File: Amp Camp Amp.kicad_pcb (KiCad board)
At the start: 2 copper layers, 120 x 111.2 mm, 58 parts, among them Q1 IRFP240, Q2 IRFP240, Q3 ZTX450, Q4 2SK170, SW1 MONO, T1 IN_L_P5.00mm, T2 OUT_L_P5.00mm, T3 S+24V_IN_L_P5.00mm, T4 IN_L_P5.00mm, T5 IN_R_P5.00mm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

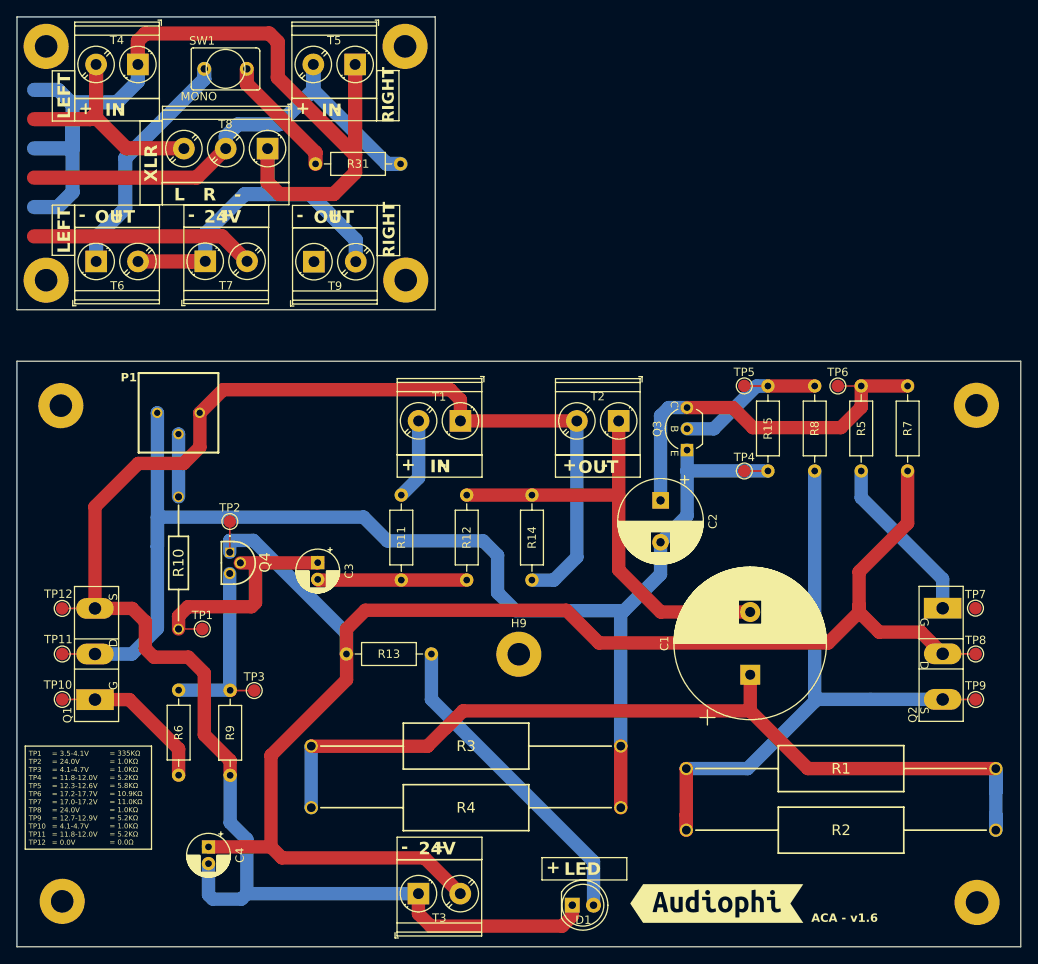
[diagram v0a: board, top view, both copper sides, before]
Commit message: Updated the board to version 1.8
List of all differences between V1.6 and V1.8:

Rear switch is a 3 position DPDT instead of 2 position, necessitating a change in wiring
Rear panel is printed with a connection diagram
Chassis rails are improved using weld nuts and secured by bolts
Blade terminals are included for the front power switch
Longer wire
LED resistors have been changed from 10k to 33.2k to reduce LED brightness
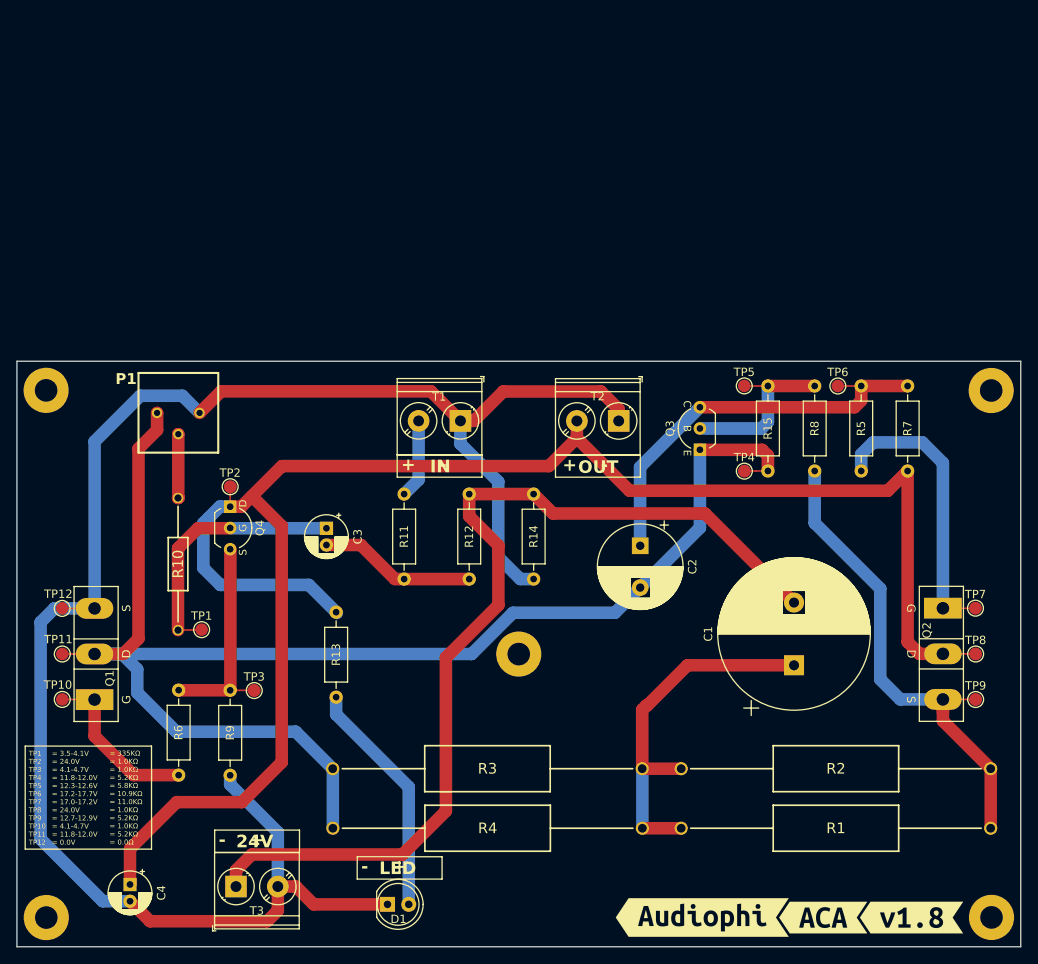
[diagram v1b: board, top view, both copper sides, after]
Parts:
- removed H6, H7, H8, H9: MountingHole_Pad, MountingHole:MountingHole_2.7mm_Pad
- removed R31: 39k, Resistor_THT:R_Axial_DIN0207_L6.3mm_D2.5mm_P10.16mm_Horizontal
- removed SW1: MONO, PCM_4ms_Switch:Switch_Toggle_SPST_SubMini
- removed T4: IN_L_P5.00mm, TerminalBlock_Phoenix:TerminalBlock_Phoenix_PT-1,5-2-5.0-H_1x02_P5.00mm_Horizontal
- removed T5: IN_R_P5.00mm, TerminalBlock_Phoenix:TerminalBlock_Phoenix_PT-1,5-2-5.0-H_1x02_P5.00mm_Horizontal
- removed T6: OUT_L_P5.00mm, TerminalBlock_Phoenix:TerminalBlock_Phoenix_PT-1,5-2-5.0-H_1x02_P5.00mm_Horizontal
- removed T7: IN+24V_P5.00mm, TerminalBlock_Phoenix:TerminalBlock_Phoenix_PT-1,5-2-5.0-H_1x02_P5.00mm_Horizontal
- removed T8: XLR_IN_P5.00mm, TerminalBlock_Phoenix:TerminalBlock_Phoenix_PT-1,5-3-5.0-H_1x03_P5.00mm_Horizontal
- removed T9: OUT_R_P5.00mm, TerminalBlock_Phoenix:TerminalBlock_Phoenix_PT-1,5-2-5.0-H_1x02_P5.00mm_Horizontal
- removed VR1: 3386P-1-502LF, Samacsys:3386P_1
- added P1: 3386P-1-502LF, Samacsys:3386P_1, B.Cu at (118.9, 85.2)
- added kibuzzard-674CED68: G***, kibuzzard-674CED68, F.Cu at (200.8, 150.3)
- added kibuzzard-674D924F: G***, kibuzzard-674D924F, F.Cu at (211.4, 150.3)
- Q4: value 2SK170 -> TO-92_Inline_Wide_EBC; footprint Samacsys:2SK170 -> PCM_Package_TO_SOT_THT_AKL:TO-92_Inline_Wide_EBC
- R13: value 10k Ω -> 33.2k
- T2: value OUT_L_P5.00mm -> S+24V_IN_L_P5.00mm
- T3: value S+24V_IN_L_P5.00mm -> OUT_L_P5.00mm
- TP11: value 11.8-12V/5.2KΩ -> 12V (BIAS)
- TP12: value 0V/0Ω -> 0V
- TP4: value 11.8-12V -> 12V
- TP5: value 12.3-12.6V -> 12.6V
- TP7: value 17.0-17.2V -> 17.2-17.7V
- TP9: value 12.7-12.9V -> 12.9V
- moved H4 103.5 mm to (220.9, 150.2)
- moved H2 81.3 mm to (220.9, 87.3)
- moved H3 76.2 mm to (107.9, 150.3)
- moved H5 62.3 mm to (164.4, 118.8)
- moved H1 41.1 mm to (107.9, 87.2)
- moved R4 39.7 mm to (179.2, 139.6), turned to 180 degrees
- moved R3 39.7 mm to (179.2, 132.5), turned to 180 degrees
- moved R2 37.1 mm to (220.8, 132.5), turned to 180 degrees
- moved R1 37.1 mm to (220.8, 139.6), turned to 180 degrees
- moved D1 22.1 mm to (148.7, 148.7)
- moved T3 21.8 mm to (130.6, 146.6)
- moved C4 10.4 mm to (117.9, 146.3)
- moved C2 5.94 mm to (178.9, 105.8)
- moved Q4 5.45 mm to (129.9, 101.2)
- moved C1 5.36 mm to (197.3, 120.1)
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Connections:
- T2 pad 1: OUT__L- -> OUT__L+
- T2 pad 2: OUT__L+ -> +24V__LEFT
- T3 pad 1: OUT__L+ -> OUT__L-
- T3 pad 2: +24V__LEFT -> OUT__L+
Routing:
- net OUT_L+: track 150.4 -> 0.00 mm
- net Net-(C1-Pad1): track 110.1 -> 43.8 mm
- net OUT__L-: track 53.8 -> 116.1 mm
- net Net-(R31-Pad2): track 58.8 -> 0.00 mm
- net OUT_L-: track 28.4 -> 0.00 mm
- net +24V: track 26.7 -> 0.00 mm
- net Net-(T4-Pad2): track 25.9 -> 0.00 mm
- net +24V__LEFT: track 189.8 -> 209.1 mm
- net Net-(P1-CW): track 164.8 -> 181.7 mm
- net Net-(Q2-S): track 75.1 -> 59.9 mm
- net Net-(SW1-B): track 14.8 -> 0.00 mm
- net Net-(Q2-G): track 20.4 -> 34.6 mm
- net OUT__L+: track 206.9 -> 217.9 mm
- net Net-(D1-Pad2): track 38.1 -> 28.4 mm
- net Net-(Q4-G): track 28.3 -> 31.3 mm
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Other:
- board size 120 x 111.2 mm -> 120 x 70 mm
- board text removed: "+ L -"
- board text removed: "+ R -"
- board text removed: "+24V-"
- board text removed: "ACA - v1.6"
- board text removed: "L R -"
- board text removed: "LEFT"
- board text removed: "RIGHT"
- board text removed: "XLR"
